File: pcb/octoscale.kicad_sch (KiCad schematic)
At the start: 98 parts, among them J1 USB_C_Receptacle_USB2.0 TYPE-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, J2 Conn_01x04_Male, J3 JST PH Vertical C64658, J4 JST-SH, stemma, J5 JST-SH, J6 JST-SH, Q1 AO3415_C181094, Q2 MMBT44032T, Q3 S8050, SW1 SW_Push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

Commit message: first draft of case
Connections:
- net +BATT: now also J3.1 (Pin_1); no longer J3.2 (Pin_2)
- net GND: now also J3.2 (Pin_2); no longer J3.1 (Pin_1)
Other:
- moved on the sheet: J3
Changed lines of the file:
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@@
     (pin "2")
   )
-  (symbol (lib_id "Connector:Conn_01x02_Female") (at 87.376 43.942 270) (unit 1)
+  (symbol (lib_id "Connector:Conn_01x02_Female") (at 84.836 43.942 90) (mirror x) (unit 1)
     (in_bom yes) (on_board yes)
-    (property "Reference" "J3" (id 0) (at 88.646 42.0369 90)
+    (property "Reference" "J3" (id 0) (at 83.566 42.0369 90)
       (effects (font (size 1.27 1.27)) (justify left))
     )
-    (property "Value" "JST PH Vertical C64658" (id 1) (at 75.311 46.482 90)
+    (property "Value" "JST PH Vertical C64658" (id 1) (at 96.901 46.482 90)
       (effects (font (size 1.27 1.27)) (justify left))
     )
-    (property "Footprint" "Connector_JST:JST_PH_B2B-PH-SM4-TB_1x02-1MP_P2.00mm_Vertical" (id 2) (at 87.376 43.942 0)
+    (property "Footprint" "Connector_JST:JST_PH_B2B-PH-SM4-TB_1x02-1MP_P2.00mm_Vertical" (id 2) (at 84.836 43.942 0)
       (effects (font (size 1.27 1.27)) hide)
     )
-    (property "Datasheet" "~" (id 3) (at 87.376 43.942 0)
+    (property "Datasheet" "~" (id 3) (at 84.836 43.942 0)
       (effects (font (size 1.27 1.27)) hide)
     )

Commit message: Change battery connector and load cell
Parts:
- added J7: Conn_01x04_Male, Connector_JST:JST_SH_BM04B-SRSS-TB_1x04-1MP_P1.00mm_Vertical, symbol Connector:Conn_01x04_Male
- J3: value JST PH Vertical C64658 -> Molex picoblade vertical C122410; footprint Connector_JST:JST_PH_B2B-PH-SM4-TB_1x02-1MP_P2.00mm_Vertical -> Connector_Molex:Molex_PicoBlade_53398-0271_1x02-1MP_P1.25mm_Vertical
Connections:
- net A+: now also J7.4 (Pin_4)
- net A-: now also J7.3 (Pin_3)
- net ADD: now also J7.1 (Pin_1)
- net GND: now also J7.2 (Pin_2)
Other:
- moved on the sheet: C10, C4, C5, C6, C7, C8, C9, J2, JP1, L1, Q2, R10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

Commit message: Tweak height clearance
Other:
- note added: "battery: 502060 lipo 600 mah"
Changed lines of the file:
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@@
     (effects (font (size 4 4) (thickness 1) bold italic) (justify left bottom))
+  )
+  (text "battery: 502060 lipo 600 mah\n" (at 72.644 50.038 0)
+    (effects (font (size 1.27 1.27)) (justify left bottom))
   )
   (text "Display" (at 351.155 128.905 0)

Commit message: Change oled to ssd1306 and fix hx711 agnd
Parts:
- added C28: 10uF, Capacitor_SMD:C_0805_2012Metric_Pad1.18x1.45mm_HandSolder, symbol Device:C_Small
- added C29: 1uF, Capacitor_SMD:C_0805_2012Metric_Pad1.18x1.45mm_HandSolder, symbol Device:C_Small
- C15, C16: value 1uF -> 2.2uF
- C17: value 4.7uF -> 10uF
- C18: value 2.2uF -> 10uF
- R17: value 400k -> 300k
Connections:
- net +3V3: now also DS1.13 (~{CS}), C28.2, C29.1
- net GND: now also C7.1, DS1.10 (BS0), R9.2, U4.5 (AGND), C28.1, C29.2; no longer DS1.13 (~{CS}), DS1.16 (R/~{W}), DS1.17 (E/~{RD}), DS1.20 (D2), DS1.21 (D3), DS1.22 (D4), DS1.23 (D5), DS1.24 (D6), DS1.25 (D7)
- net SDA: now also DS1.20 (D2)
- no-connect marks 7 -> 14
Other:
- note added: "SSD1306 1.3" 128x64 https://learn.adafruit.com/assets/87763 https://www.aliexpress.com/item/32833902623.html?spm=a2g0o.productlist.0.0.161e9124agGbN2&algo_pvid=128955a3-e0d0-4f90-829f-11a06950333c&algo_exp_id=128955a3-e0d0-4f90-829f-11a06950333c-10&pdp_ext_f=%7B%22sku_id%22%3A%2265420055737%22%7D&pdp_npi=2%40dis%21GBP%21%212.32%212.32%21%211.99%21%21%402100bdd816544379130082450eea22%2165420055737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"

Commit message: Move touch 2 pins
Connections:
- net BATT_SENSE: now also U5.23 (GPIO21); no longer U5.21 (GPIO13/TOUCH13/ADC2_CH2/FSPIQ/FSPIIO7/SUBSPIQ)
- net OLED_RESET: now also U5.22 (GPIO14/TOUCH14/ADC2_CH3/FSPIWP/FSPIDQS/SUBSPIWP); no longer U5.20 (GPIO12/TOUCH11/ADC2_CH0/FSPICS0/FSPIIO4/SUBSPICS0)
- net POWER_SWITCH_SENSE: now also U5.24 (GPIO47/SPICLK_P/SUBSPICLK_P_DIFF); no longer U5.22 (GPIO14/TOUCH14/ADC2_CH3/FSPIWP/FSPIDQS/SUBSPIWP)
- net SCALE_DATA: now also U5.25 (GPIO48/SPICLK_N/SUBSPICLK_N_DIFF); no longer U5.23 (GPIO21)
- net SCL: now also U5.21 (GPIO13/TOUCH13/ADC2_CH2/FSPIQ/FSPIIO7/SUBSPIQ); no longer U5.19 (GPIO11/TOUCH11/ADC2_CH0/FSPICS0/FSPIIO4/SUBSPICS0)
- net SDA: now also U5.20 (GPIO12/TOUCH11/ADC2_CH0/FSPICS0/FSPIIO4/SUBSPICS0); no longer U5.18 (GPIO10/TOUCH10/ADC1_CH9/FSPICS0/FSPIIO4/SUBSPICS0)
- net CHRG: now reaches D5.1 (K), U1.1 (CHRG)
- net CHRG: now also U5.19 (GPIO11/TOUCH11/ADC2_CH0/FSPICS0/FSPIIO4/SUBSPICS0)
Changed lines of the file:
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@@
   (junction (at 254 216.535) (diameter 0) (color 0 0 0 0)
+  )
+  (junction (at 33.274 92.71) (diameter 0) (color 0 0 0 0)
   )
   (junction (at 177.8 218.44) (diameter 0) (color 0 0 0 0)
@@
     (stroke (width 0) (type default) (color 0 0 0 0))
   )
-  (wire (pts (xy 32.385 92.71) (xy 33.655 92.71))
+  (wire (pts (xy 32.385 92.71) (xy 33.274 92.71))
     (stroke (width 0) (type default) (color 0 0 0 0))
   )
@@
     (stroke (width 0) (type default) (color 0 0 0 0))
   )
+  (wire (pts (xy 33.274 92.71) (xy 33.274 94.234))
+    (stroke (width 0) (type default) (color 0 0 0 0))
+  )
   (wire (pts (xy 93.345 272.415) (xy 93.345 274.955))
     (stroke (width 0) (type default) (color 0 0 0 0))
@@
   )
   (wire (pts (xy 343.154 169.672) (xy 343.154 179.832))
+    (stroke (width 0) (type default) (color 0 0 0 0))
+  )
+  (wire (pts (xy 33.274 92.71) (xy 33.655 92.71))
     (stroke (width 0) (type default) (color 0 0 0 0))
   )
@@
     (effects (font (size 1.27 1.27)) (justify left bottom))
   )
+  (global_label "CHRG" (shape input) (at 33.274 94.234 270) (fields_autoplaced)
+    (effects (font (size 1.27 1.27)) (justify right))
+    (property "Intersheet References" "${INTERSHEET_REFS}" (id 0) (at 33.1946 101.7876 90)
+      (effects (font (size 1.27 1.27)) (justify right) hide)
+    )
+  )
   (global_label "D-" (shape input) (at 43.815 35.56 0) (fields_autoplaced)
     (effects (font (size 1.27 1.27)) (justify left))
@@
     )
   )
-  (global_label "OLED_RESET" (shape input) (at 59.69 193.04 180) (fields_autoplaced)
-    (effects (font (size 1.27 1.27)) (justify right))
-    (property "Intersheet References" "${INTERSHEET_REFS}" (id 0) (at 45.7864 192.9606 0)
+  (global_label "OLED_RESET" (shape input) (at 59.69 198.12 180) (fields_autoplaced)
+    (effects (font (size 1.27 1.27)) (justify right))
+    (property "Intersheet References" "${INTERSHEET_REFS}" (id 0) (at 45.7864 198.0406 0)
       (effects (font (size 1.27 1.27)) (justify right) hide)
     )
@@
     )
   )
-  (global_label "SCL" (shape input) (at 59.69 190.5 180) (fields_autoplaced)
-    (effects (font (size 1.27 1.27)) (justify right))
-    (property "Intersheet References" "${INTERSHEET_REFS}" (id 0) (at 53.7693 190.4206 0)
+  (global_label "SCL" (shape input) (at 59.69 195.58 180) (fields_autoplaced)
+    (effects (font (size 1.27 1.27)) (justify right))
+    (property "Intersheet References" "${INTERSHEET_REFS}" (id 0) (at 53.7693 195.5006 0)
       (effects (font (size 1.27 1.27)) (justify right) hide)
     )
@@
     )
   )
-  (global_label "SDA" (shape input) (at 59.69 187.96 180) (fields_autoplaced)
-    (effects (font (size 1.27 1.27)) (justify right))
-    (property "Intersheet References" "${INTERSHEET_REFS}" (id 0) (at 53.7088 187.8806 0)
+  (global_label "SDA" (shape input) (at 59.69 193.04 180) (fields_autoplaced)
+    (effects (font (size 1.27 1.27)) (justify right))
+    (property "Intersheet References" "${INTERSHEET_REFS}" (id 0) (at 53.7088 192.9606 0)
+      (effects (font (size 1.27 1.27)) (justify right) hide)
+    )
+  )
+  (global_label "CHRG" (shape input) (at 59.69 190.5 180) (fields_autoplaced)
+    (effects (font (size 1.27 1.27)) (justify right))
+    (property "Intersheet References" "${INTERSHEET_REFS}" (id 0) (at 52.1364 190.4206 0)
       (effects (font (size 1.27 1.27)) (justify right) hide)
     )
@@
     )
   )
-  (global_label "POWER_SWITCH_SENSE" (shape input) (at 59.69 198.12 180) (fields_autoplaced)
-    (effects (font (size 1.27 1.27)) (justify right))
-    (property "Intersheet References" "${INTERSHEET_REFS}" (id 0) (at 35.9893 198.0406 0)
-      (effects (font (size 1.27 1.27)) (justify right) hide)
+  (global_label "POWER_SWITCH_SENSE" (shape input) (at 177.8 184.15 0) (fields_autoplaced)
+    (effects (font (size 1.27 1.27)) (justify left))
+    (property "Intersheet References" "${INTERSHEET_REFS}" (id 0) (at 201.5007 184.2294 0)
+      (effects (font (size 1.27 1.27)) (justify left) hide)
     )
   )
@@
     )
   )
-  (global_label "BATT_SENSE" (shape input) (at 59.69 195.58 180) (fields_autoplaced)
-    (effects (font (size 1.27 1.27)) (justify right))
-    (property "Intersheet References" "${INTERSHEET_REFS}" (id 0) (at 45.9679 195.5006 0)
-      (effects (font (size 1.27 1.27)) (justify right) hide)
+  (global_label "BATT_SENSE" (shape input) (at 177.8 173.99 0) (fields_autoplaced)
+    (effects (font (size 1.27 1.27)) (justify left))
+    (property "Intersheet References" "${INTERSHEET_REFS}" (id 0) (at 191.5221 174.0694 0)
+      (effects (font (size 1.27 1.27)) (justify left) hide)
     )
   )
@@
     )
   )
-  (global_label "SCALE_DATA" (shape input) (at 177.8 173.99 0) (fields_autoplaced)
-    (effects (font (size 1.27 1.27)) (justify left))
-    (property "Intersheet References" "${INTERSHEET_REFS}" (id 0) (at 191.3407 174.0694 0)
-      (effects (font (size 1.27 1.27)) (justify left) hide)
-    )
+  (global_label "SCALE_DATA" (shape input) (at 177.8 181.61 0) (fields_autoplaced)
+    (effects (font (size 1.27 1.27)) (justify left))
+    (property "Intersheet References" "${INTERSHEET_REFS}" (id 0) (at 191.3407 181.6894 0)
+      (effects (font (size 1.27 1.27)) (justify left) hide)
+    )

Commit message: Add batt_sense test point
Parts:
- added TP13: TestPoint, TestPoint:TestPoint_Pad_D1.5mm, symbol Connector:TestPoint
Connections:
- net BATT_SENSE: now also TP13.1
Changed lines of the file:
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@@
     (pin "2")
+  )
+  (symbol (lib_id "Connector:TestPoint") (at 56.642 61.214 90) (unit 1)
+    (in_bom yes) (on_board yes) (fields_autoplaced)
+    (property "Reference" "TP13" (id 0) (at 53.34 55.88 90))
+    (property "Value" "TestPoint" (id 1) (at 53.34 58.42 90))
+    (property "Footprint" "TestPoint:TestPoint_Pad_D1.5mm" (id 2) (at 56.642 56.134 0)
+      (effects (font (size 1.27 1.27)) hide)
+    )
+    (property "Datasheet" "~" (id 3) (at 56.642 56.134 0)
+      (effects (font (size 1.27 1.27)) hide)
+    )
+    (pin "1")
   )
   (symbol (lib_id "power:+BATT") (at 93.345 254.635 0) (unit 1)
@@
       (reference "TP12") (unit 1) (value "TestPoint") (footprint "TestPoint:TestPoint_Pad_D1.5mm")
     )
+    (path "/b6e871d1-589a-4c01-92d5-10276bde3831"
+      (reference "TP13") (unit 1) (value "TestPoint") (footprint "TestPoint:TestPoint_Pad_D1.5mm")
+    )
     (path "/717c666a-71be-4f20-a086-8c131f43aa8f"

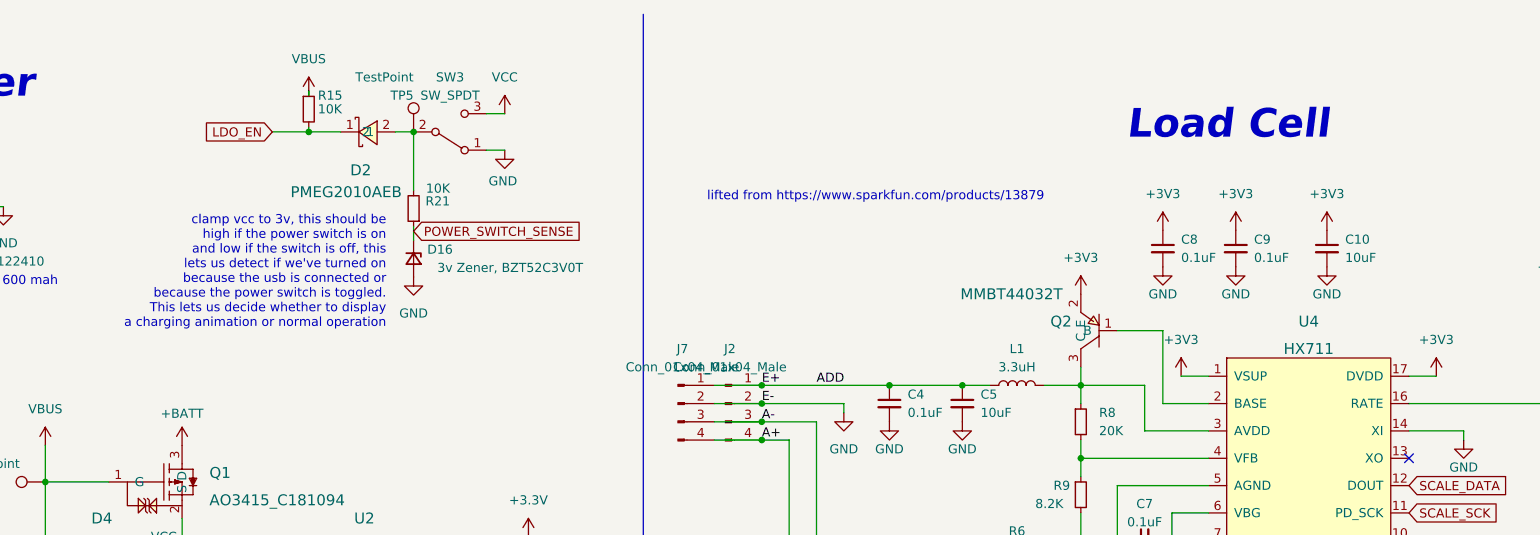
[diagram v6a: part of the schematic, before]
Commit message: Tweak to layout and power ldo en
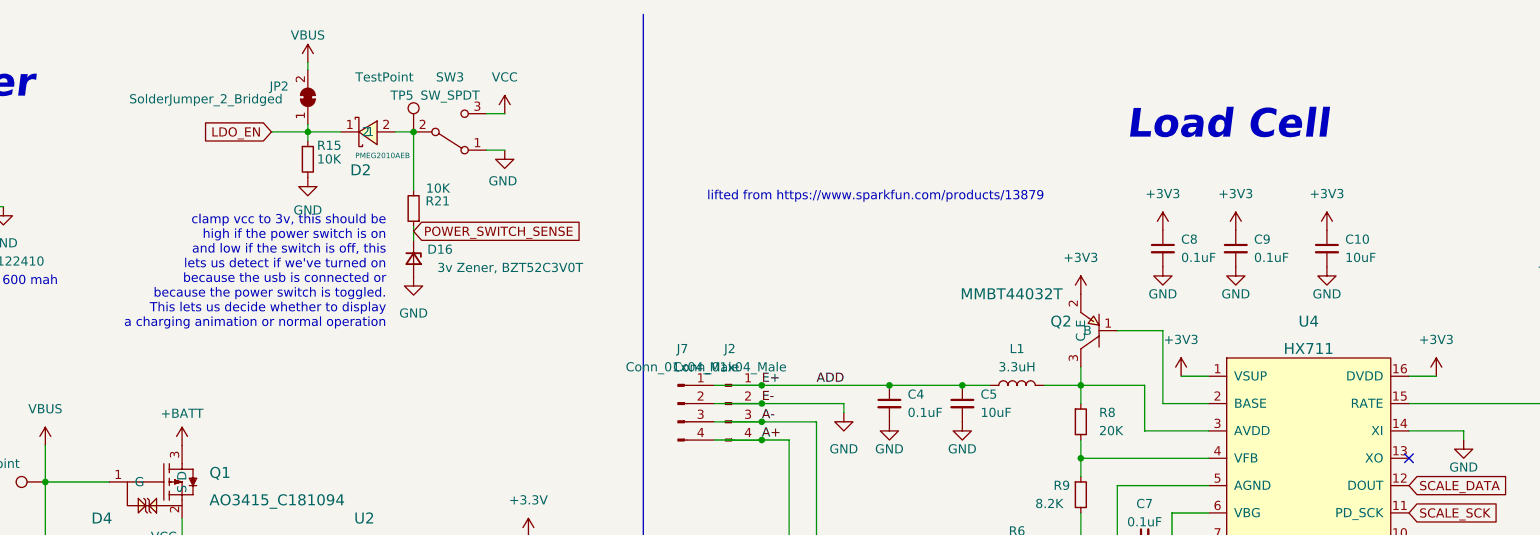
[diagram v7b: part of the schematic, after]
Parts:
- added JP2: SolderJumper_2_Bridged, SolderJumper-2_P1.3mm_Bridged_RoundedPad1.0x1.5mm, symbol Jumper:SolderJumper_2_Bridged
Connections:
- net +3V3: now also U4.16 (DVDD); no longer U4.17 (DVDD)
- net GND: now also R15.2
- net LDO_EN: now also R15.1, JP2.1 (A); no longer R15.2
- net VBUS: now also JP2.2 (B); no longer R15.1
- net at JP1.2 (B), R10.2: now also U4.15 (RATE); no longer U4.16 (RATE)
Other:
- moved on the sheet: R15
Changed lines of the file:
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@@
   (junction (at 208.28 269.875) (diameter 0) (color 0 0 0 0)
   )
+  (junction (at 133.604 28.448) (diameter 0) (color 0 0 0 0)
+  )
   (junction (at 179.07 168.91) (diameter 0) (color 0 0 0 0)
   )
@@
   (junction (at 343.154 215.392) (diameter 0) (color 0 0 0 0)
   )
-  (junction (at 133.731 28.448) (diameter 0) (color 0 0 0 0)
-  )
   (junction (at 343.154 179.832) (diameter 0) (color 0 0 0 0)
   )
@@
     (stroke (width 0) (type default) (color 0 0 0 0))
   )
+  (wire (pts (xy 133.604 18.796) (xy 133.604 19.812))
+    (stroke (width 0) (type default) (color 0 0 0 0))
+  )
   (wire (pts (xy 32.385 92.71) (xy 33.274 92.71))
     (stroke (width 0) (type default) (color 0 0 0 0))
@@
     (stroke (width 0) (type default) (color 0 0 0 0))
   )
-  (wire (pts (xy 133.731 22.733) (xy 133.731 23.368))
-    (stroke (width 0) (type default) (color 0 0 0 0))
-  )
   (wire (pts (xy 65.405 272.415) (xy 80.645 272.415))
     (stroke (width 0) (type default) (color 0 0 0 0))
@@
     (stroke (width 0) (type default) (color 0 0 0 0))
   )
+  (wire (pts (xy 133.604 28.448) (xy 133.604 29.718))
+    (stroke (width 0) (type default) (color 0 0 0 0))
+  )
   (polyline (pts (xy 299.72 184.15) (xy 299.72 183.515))
     (stroke (width 0) (type default) (color 0 0 0 0))
@@
     (stroke (width 0) (type default) (color 0 0 0 0))
   )
-  (wire (pts (xy 133.731 28.448) (xy 138.176 28.448))
-    (stroke (width 0) (type default) (color 0 0 0 0))
-  )
   (wire (pts (xy 43.815 26.67) (xy 60.325 26.67))
     (stroke (width 0) (type default) (color 0 0 0 0))
@@
     (stroke (width 0) (type default) (color 0 0 0 0))
   )
+  (wire (pts (xy 133.604 28.448) (xy 138.176 28.448))
+    (stroke (width 0) (type default) (color 0 0 0 0))
+  )
   (wire (pts (xy 156.718 89.916) (xy 164.338 89.916))
     (stroke (width 0) (type default) (color 0 0 0 0))
@@
     (stroke (width 0) (type default) (color 0 0 0 0))
   )
-  (wire (pts (xy 133.731 27.813) (xy 133.731 28.448))
-    (stroke (width 0) (type default) (color 0 0 0 0))
-  )
   (wire (pts (xy 350.774 195.072) (xy 347.218 195.072))
     (stroke (width 0) (type default) (color 0 0 0 0))
@@
     (stroke (width 0) (type default) (color 0 0 0 0))
   )
+  (wire (pts (xy 128.524 28.448) (xy 133.604 28.448))
+    (stroke (width 0) (type default) (color 0 0 0 0))
+  )
   (wire (pts (xy 272.415 275.59) (xy 274.955 275.59))
     (stroke (width 0) (type default) (color 0 0 0 0))
@@
     (stroke (width 0) (type default) (color 0 0 0 0))
   )
-  (wire (pts (xy 128.651 28.448) (xy 133.731 28.448))
-    (stroke (width 0) (type default) (color 0 0 0 0))
-  )
   (wire (pts (xy 246.38 94.234) (xy 257.81 94.234))
     (stroke (width 0) (type default) (color 0 0 0 0))
@@
     (stroke (width 0) (type default) (color 0 0 0 0))
   )
+  (wire (pts (xy 133.604 27.432) (xy 133.604 28.448))
+    (stroke (width 0) (type default) (color 0 0 0 0))
+  )
   (wire (pts (xy 343.154 169.672) (xy 343.154 179.832))
     (stroke (width 0) (type default) (color 0 0 0 0))
@@
     )
   )
-  (global_label "LDO_EN" (shape input) (at 128.651 28.448 180) (fields_autoplaced)
+  (global_label "LDO_EN" (shape input) (at 128.524 28.448 180) (fields_autoplaced)
     (effects (font (size 1.27 1.27)) (justify right))
-    (property "Intersheet References" "${INTERSHEET_REFS}" (id 0) (at 119.1622 28.3686 0)
+    (property "Intersheet References" "${INTERSHEET_REFS}" (id 0) (at 119.0352 28.3686 0)
       (effects (font (size 1.27 1.27)) (justify right) hide)
     )
@@
     (pin "13")
     (pin "14")
+    (pin "15")
     (pin "16")
-    (pin "17")
     (pin "2")
     (pin "3")
@@
     (pin "2")
   )
-  (symbol (lib_id "Device:R_Small") (at 133.731 25.273 0) (unit 1)
+  (symbol (lib_id "Device:R_Small") (at 133.604 32.258 0) (unit 1)
     (in_bom yes) (on_board yes)
-    (property "Reference" "R15" (id 0) (at 135.001 23.368 0)
+    (property "Reference" "R15" (id 0) (at 134.874 30.353 0)
       (effects (font (size 1.27 1.27)) (justify left))
     )
-    (property "Value" "10K" (id 1) (at 135.001 25.273 0)
+    (property "Value" "10K" (id 1) (at 134.874 32.258 0)
       (effects (font (size 1.27 1.27)) (justify left))
     )
-    (property "Footprint" "Resistor_SMD:R_0805_2012Metric_Pad1.20x1.40mm_HandSolder" (id 2) (at 133.731 25.273 0)
+    (property "Footprint" "Resistor_SMD:R_0805_2012Metric_Pad1.20x1.40mm_HandSolder" (id 2) (at 133.604 32.258 0)
       (effects (font (size 1.27 1.27)) hide)
     )
-    (property "Datasheet" "~" (id 3) (at 133.731 25.273 0)
+    (property "Datasheet" "~" (id 3) (at 133.604 32.258 0)
       (effects (font (size 1.27 1.27)) hide)
     )
@@
     (pin "1")
   )
+  (symbol (lib_id "power:GND") (at 133.604 34.798 0) (unit 1)
+    (in_bom yes) (on_board yes) (fields_autoplaced)
+    (property "Reference" "#PWR0121" (id 0) (at 133.604 41.148 0)
+      (effects (font (size 1.27 1.27)) hide)
+    )
+    (property "Value" "GND" (id 1) (at 133.604 39.37 0))
+    (property "Footprint" "" (id 2) (at 133.604 34.798 0)
+      (effects (font (size 1.27 1.27)) hide)
+    )
+    (property "Datasheet" "" (id 3) (at 133.604 34.798 0)
+      (effects (font (size 1.27 1.27)) hide)
+    )
+    (pin "1")
+  )
   (symbol (lib_id "power:GND") (at 282.575 261.62 0) (unit 1)
     (in_bom yes) (on_board yes) (fields_autoplaced)
@@
     (pin "1")
   )
-  (symbol (lib_id "power:VBUS") (at 133.731 23.368 0) (unit 1)
-    (in_bom yes) (on_board yes) (fields_autoplaced)
-    (property "Reference" "#PWR0117" (id 0) (at 133.731 27.178 0)
+  (symbol (lib_id "power:VBUS") (at 133.604 18.796 0) (unit 1)
+    (in_bom yes) (on_board yes)
+    (property "Reference" "#PWR0117" (id 0) (at 133.604 22.606 0)
       (effects (font (size 1.27 1.27)) hide)
     )
-    (property "Value" "VBUS" (id 1) (at 133.731 18.288 0))
-    (property "Footprint" "" (id 2) (at 133.731 23.368 0)
+    (property "Value" "VBUS" (id 1) (at 133.604 14.986 0))
+    (property "Footprint" "" (id 2) (at 133.604 18.796 0)
       (effects (font (size 1.27 1.27)) hide)
     )
-    (property "Datasheet" "" (id 3) (at 133.731 23.368 0)
+    (property "Datasheet" "" (id 3) (at 133.604 18.796 0)
       (effects (font (size 1.27 1.27)) hide)
     )
@@
       (effects (font (size 1.524 1.524)))
     )
-    (property "Value" "PMEG2010AEB" (id 1) (at 138.938 36.83 0)
-      (effects (font (size 1.524 1.524)))
+    (property "Value" "PMEG2010AEB" (id 1) (at 144.018 31.75 0)
+      (effects (font (size 0.75 0.75)))
     )
     (property "Footprint" "Diode_SMD:D_SOD-523" (id 2) (at 141.986 36.068 0)
@@
     (pin "1")
   )
+  (symbol (lib_id "Jumper:SolderJumper_2_Bridged") (at 133.604 23.622 90) (unit 1)
+    (in_bom yes) (on_board yes)
+    (property "Reference" "JP2" (id 0) (at 128.27 22.098 90)
+      (effects (font (size 1.27 1.27)) (justify right))
+    )
+    (property "Value" "SolderJumper_2_Bridged" (id 1) (at 108.712 23.876 90)
+      (effects (font (size 1.27 1.27)) (justify right))
+    )
+    (property "Footprint" "SolderJumper-2_P1.3mm_Bridged_RoundedPad1.0x1.5mm" (id 2) (at 133.604 23.622 0)
+      (effects (font (size 1.27 1.27)) hide)
+    )
+    (property "Datasheet" "~" (id 3) (at 133.604 23.622 0)
+      (effects (font (size 1.27 1.27)) hide)
+    )
+    (pin "1")
+    (pin "2")
+  )
   (symbol (lib_id "easyeda2kicad:MSK4005") (at 104.648 89.916 180) (unit 1)
     (in_bom yes) (on_board yes) (fields_autoplaced)
@@
       (reference "#PWR0120") (unit 1) (value "+3.3V") (footprint "")
     )
+    (path "/783e15dd-a30c-46e4-a5f1-3cbecaf74ff2"
+      (reference "#PWR0121") (unit 1) (value "GND") (footprint "")
+    )
     (path "/1db15975-65e7-4582-b6d2-4fa8d6ed3782"
       (reference "C1") (unit 1) (value "10uF") (footprint "Capacitor_SMD:C_0805_2012Metric_Pad1.18x1.45mm_HandSolder")
@@
       (reference "JP1") (unit 1) (value "Default: Open") (footprint "Jumper:SolderJumper-2_P1.3mm_Open_TrianglePad1.0x1.5mm")
     )
+    (path "/fd6e8f97-3626-420e-8c24-4a9a91138c41"
+      (reference "JP2") (unit 1) (value "SolderJumper_2_Bridged") (footprint "SolderJumper-2_P1.3mm_Bridged_RoundedPad1.0x1.5mm")
+    )
     (path "/055e53a3-5962-4f31-92ff-64f5300dbf30"
